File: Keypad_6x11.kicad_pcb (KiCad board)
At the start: 2 copper layers, 190 x 100 mm, 139 parts, among them J1 Conn_02x10_Odd_Even, SW1 SW_Push, SW10 SW_Push, SW11 SW_Push, SW12 SW_Push, SW13 SW_Push, SW14 SW_Push, SW15 SW_Push, SW16 SW_Push, SW17 SW_Push, SW18 SW_Push, SW19 SW_Push, SW2 SW_Push, SW20 SW_Push, SW21 SW_Push, SW22 SW_Push, SW23 SW_Push, SW24 SW_Push, SW25 SW_Push, SW26 SW_Push, SW27 SW_Push, SW28 SW_Push, SW29 SW_Push, SW3 SW_Push, SW30 SW_Push, SW31 SW_Push, SW32 SW_Push, SW33 SW_Push, SW34 SW_Push, SW35 SW_Push, SW36 SW_Push, SW37 SW_Push, SW38 SW_Push, SW39 SW_Push, SW4 SW_Push, SW40 SW_Push, SW41 SW_Push, SW42 SW_Push, SW43 SW_Push, SW44 SW_Push, SW45 SW_Push, SW46 SW_Push, SW47 SW_Push, SW48 SW_Push, SW49 SW_Push, SW5 SW_Push, SW50 SW_Push, SW51 SW_Push, SW52 SW_Push, SW53 SW_Push, SW54 SW_Push, SW55 SW_Push, SW56 SW_Push, SW57 SW_Push, SW58 SW_Push, SW59 SW_Push, SW6 SW_Push, SW60 SW_Push, SW61 SW_Push, SW62 SW_Push, SW63 SW_Push, SW64 SW_Push, SW65 SW_Push, SW66 SW_Push, SW7 SW_Push, SW8 SW_Push, SW9 SW_Push

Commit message: Switch to smaller SOD-323 diode footprint for SMT assembly
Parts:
- D1, D10, D11, D12, D13, D14, D15, D16, D17, D18, D19, D2, D20, D21, D22, D23, D24, D25, D26, D27, D28, D29, D3, D30, D31, D32, D33, D34, D35, D36, D37, D38, D39, D4, D40, D41, D42, D43, D44, D45, D46, D47, D48, D49, D5, D50, D51, D52, D53, D54, D55, D56, D57, D58, D59, D6, D60, D61, D62, D63, D64, D65, D66, D7, D8, D9: footprint dresco:D_SOD-323_HandSoldering -> dresco:D_SOD-323
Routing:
- net col1: track 143.5 -> 150.2 mm
- net col0: track 124.1 -> 130.8 mm
- net col4: track 189.3 -> 196.0 mm
- net col9: track 274.4 -> 281.2 mm
- net col5: track 209.0 -> 215.7 mm
- net col3: track 176.2 -> 183.0 mm
- net col2: track 156.5 -> 163.3 mm
- net col6: track 222.0 -> 228.7 mm
- net col8: track 255.2 -> 261.4 mm
- net col7: track 242.3 -> 248.4 mm
- net col10: track 290.6 -> 289.4 mm
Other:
- board text added: "github.com/dresco/grblPANEL"
- board text added: "grblPANEL - 6x11 matrix keypad"
- board text added: "v 1.01"

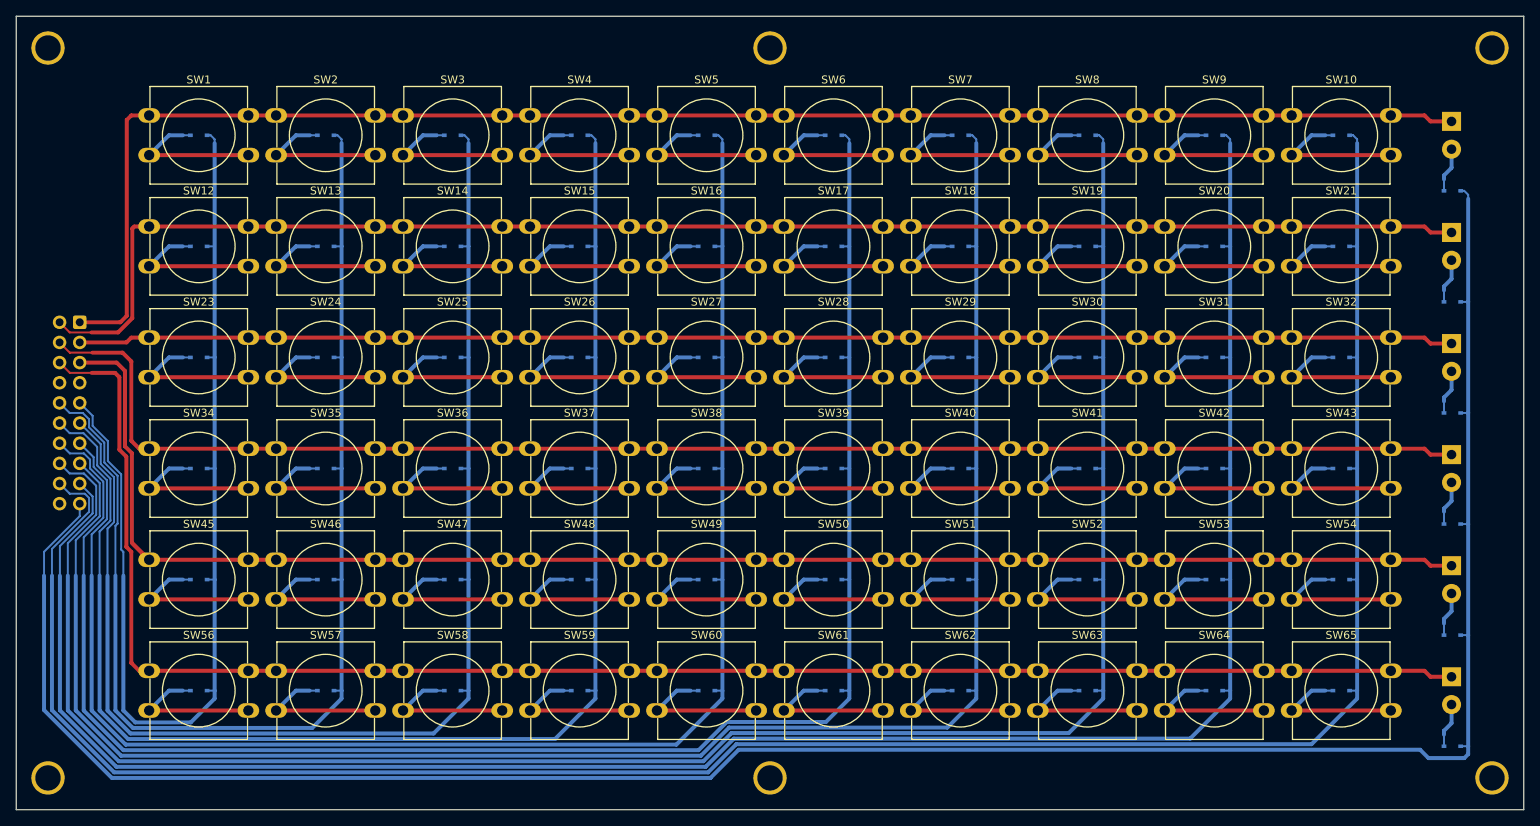
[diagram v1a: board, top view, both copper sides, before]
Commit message: Add OSHW logo, rounded board corners
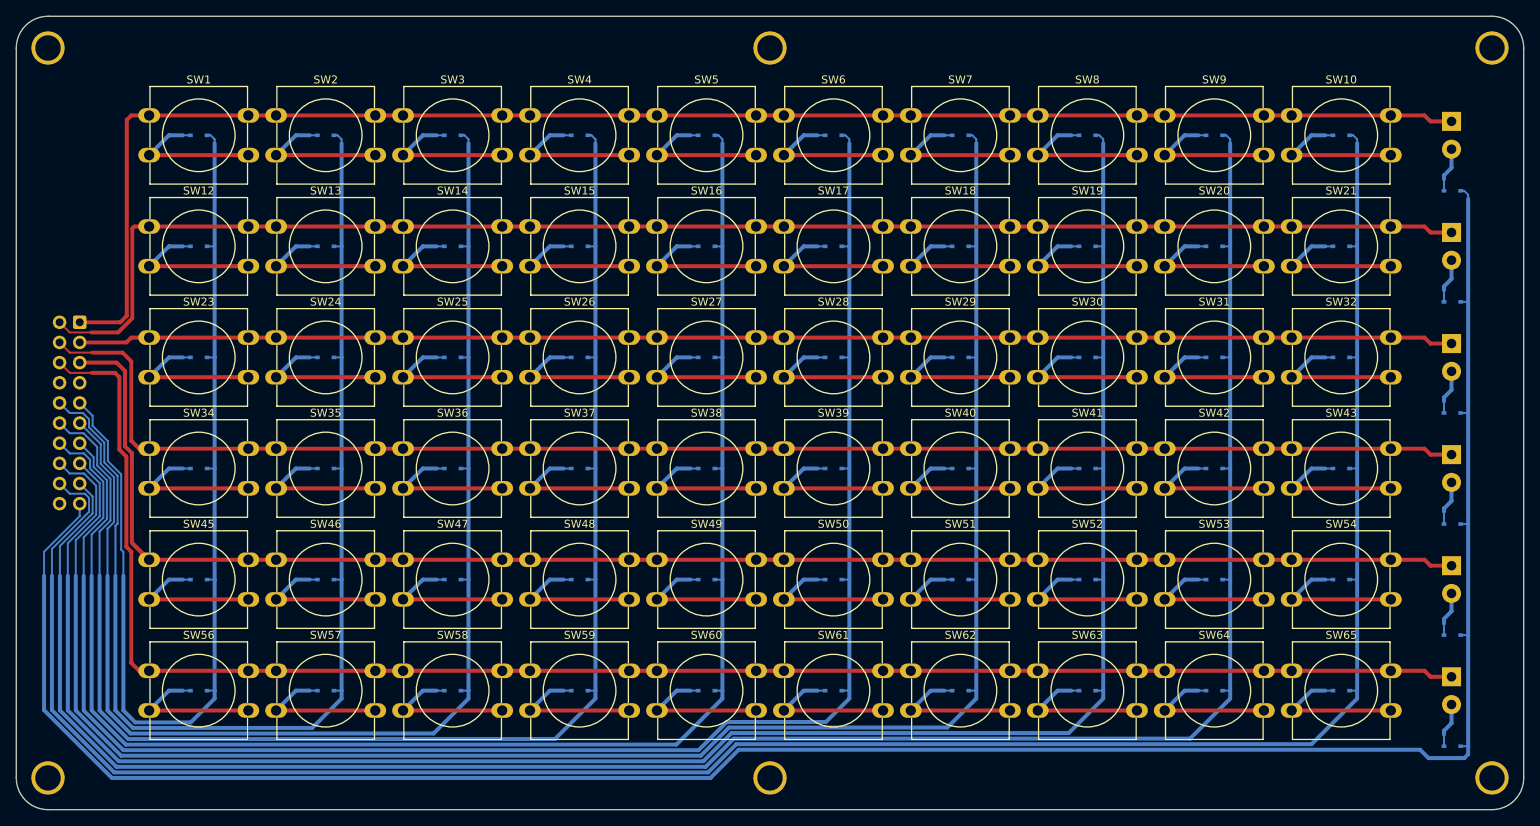
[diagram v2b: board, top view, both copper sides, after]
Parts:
- added G***: LOGO, dresco:OSHW_LOGO_10MM, B.Cu at (70.0, 49.0)
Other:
- outline, holes or cut-outs redrawn
- board text added: "v 1.02"
- board text removed: "v 1.01"

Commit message: v1.02 updates for manufacturing
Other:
- board text added: "CC-BY-SA"
- board text added: "JLCJLCJLCJLC"
- board text added: "v 1.02 - Jan '22"
- board text removed: "v 1.02"
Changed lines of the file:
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@@
   (gr_arc (start 67 130) (mid 64.171573 128.828427) (end 63 126) (layer "Edge.Cuts") (width 0.1))
   (gr_line (start 67 30) (end 249 30) (layer "Edge.Cuts") (width 0.1))
-  (gr_text "v 1.02" (at 209 126) (layer "B.SilkS")
+  (gr_text "v 1.02 - Jan '22" (at 204 126) (layer "B.SilkS")
     (effects (font (size 2 2) (thickness 0.3)) (justify mirror))
   )
-  (gr_text "github.com/dresco/grblPANEL" (at 119 34) (layer "B.SilkS")
+  (gr_text "github.com/dresco/grblPANEL" (at 115 34) (layer "B.SilkS")
     (effects (font (size 2 2) (thickness 0.3)) (justify mirror))
   )
-  (gr_text "grblPANEL - 6x11 matrix keypad" (at 208 34) (layer "B.SilkS")
+  (gr_text "grblPANEL - 6x11 matrix keypad" (at 207 34) (layer "B.SilkS")
     (effects (font (size 2 2) (thickness 0.3)) (justify mirror))
   )
+  (gr_text "CC-BY-SA" (at 70 55.5) (layer "B.SilkS")
+    (effects (font (size 2 1.5) (thickness 0.25)) (justify mirror))
+  )
+  (gr_text "JLCJLCJLCJLC" (at 65.9 80 90) (layer "B.SilkS")
+    (effects (font (size 0.8 1) (thickness 0.15)) (justify mirror))
+  )
   (segment (start 87.05 87) (end 88 87) (width 0.25) (layer "B.Cu") (net 1))
